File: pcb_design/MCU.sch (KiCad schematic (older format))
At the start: 17 parts, among them J9 SWD, SW1 BOOTLOADER, U1 STM32F40X_LQFP64, X2 ABM3B - 8MHz

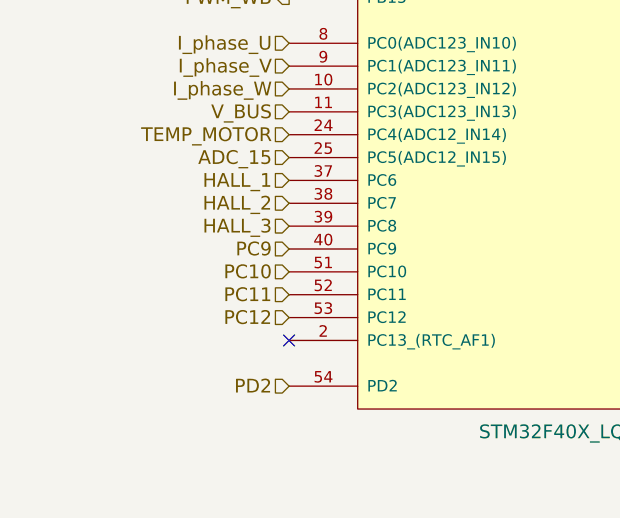
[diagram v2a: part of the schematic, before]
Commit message: Resolver routed. Added 12v regulator. The screw terminals were backwards(!). Started clearing up DRC markers.
Signed-off-by: Marcos Chaparro <mchaparro@paltatech.com>
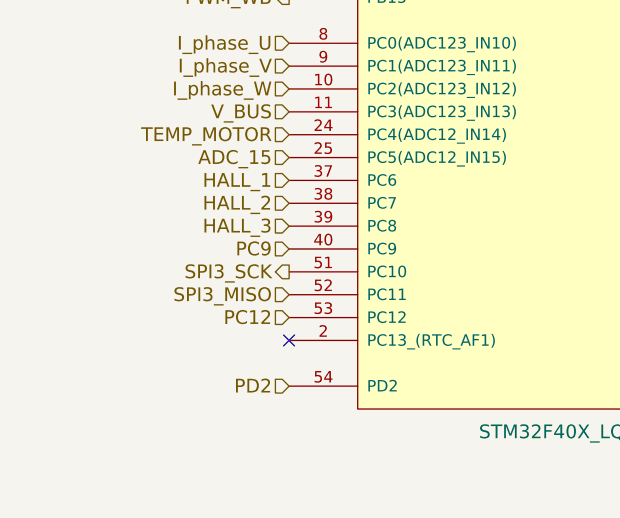
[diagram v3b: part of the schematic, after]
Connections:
- net PC10 renamed SPI3_SCK
- net PC11 renamed SPI3_MISO
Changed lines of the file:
@@
 I_phase_W
 Text HLabel 3650 5400 0    60   Input ~ 0
-PC11
-Text HLabel 3650 5500 0    60   Input ~ 0
-PC12
-Text HLabel 3650 5300 0    60   Input ~ 0
-PC10
+SPI3_MISO
+Text HLabel 3650 5300 0    60   Output ~ 0
+SPI3_SCK
 Text HLabel 3650 5200 0    60   Input ~ 0
 PC9
@@
 Text Notes 6000 2400 0    30   ~ 0
 remember it should be\npulled down if you want\nto enter bootloader
+Text HLabel 3650 5500 0    60   Input ~ 0
+PC12
 $EndSCHEMATC

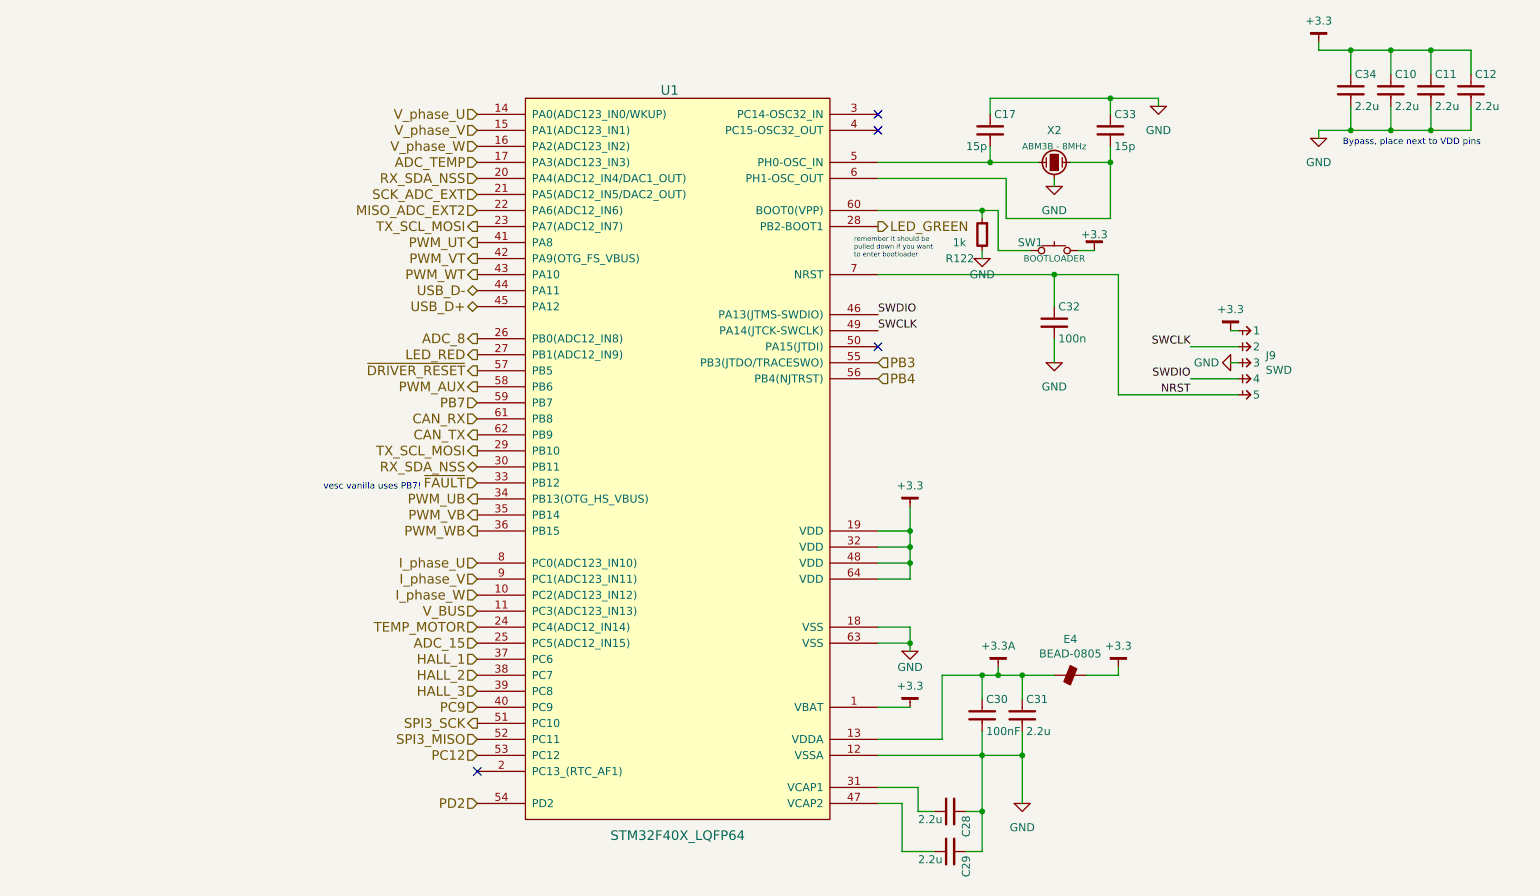
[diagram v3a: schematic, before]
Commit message: Routing complete. Added 3D models. No DRC errors, a few ERC warnings
Signed-off-by: Marcos Chaparro <mchaparro@paltatech.com>
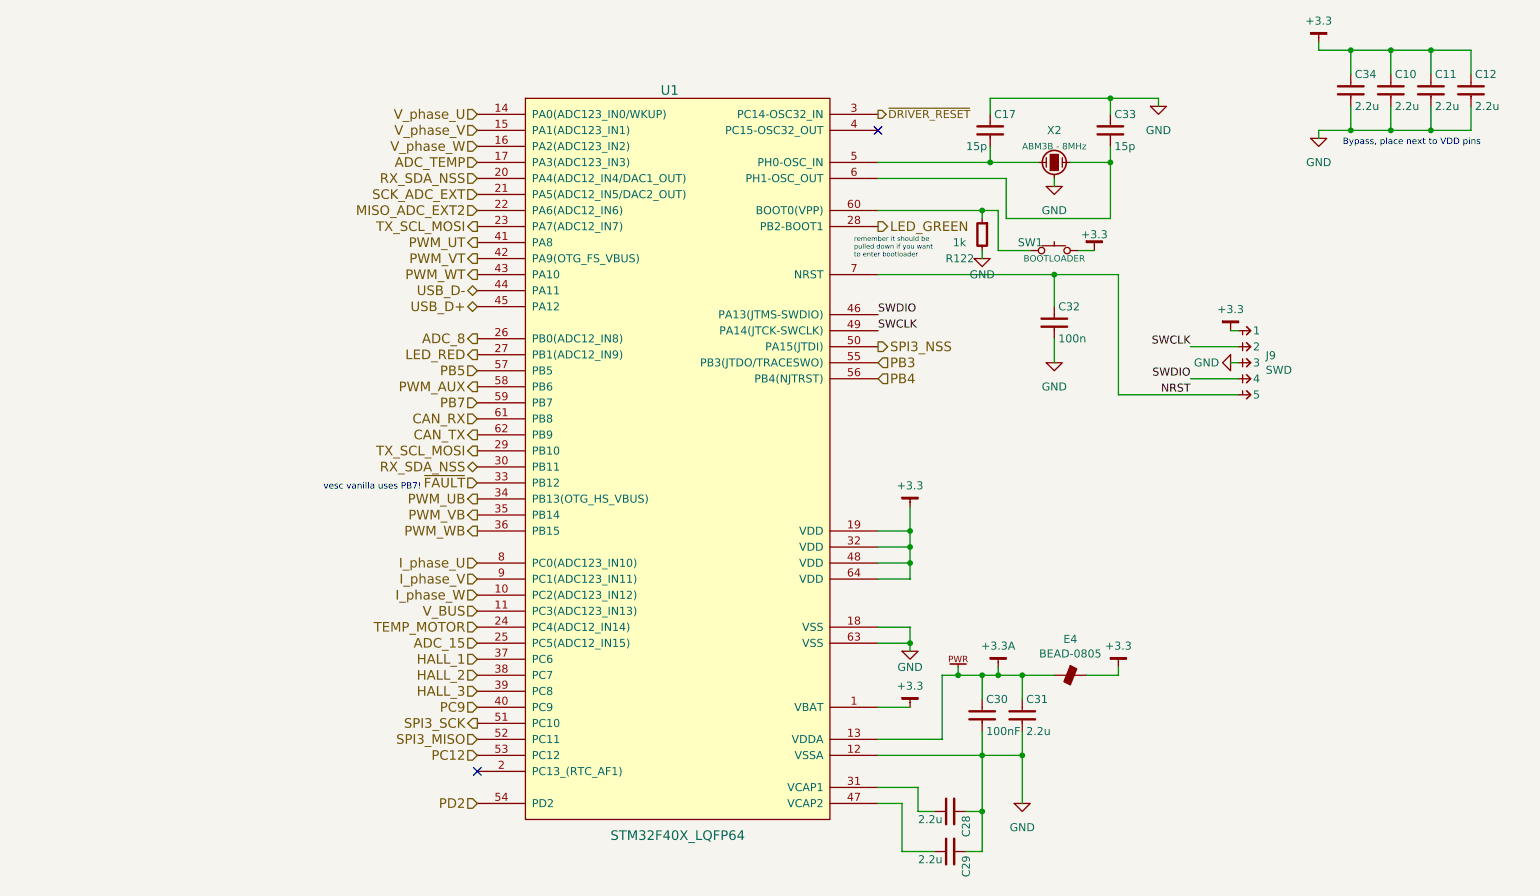
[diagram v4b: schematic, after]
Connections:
- net ~DRIVER_RESET: now also U1.3 (PC14-OSC32_IN); no longer U1.57 (PB5)
- net SPI3_NSS: now reaches U1.50 (PA15(JTDI))
- new net PB5: U1.57 (PB5)
- no-connect marks 4 -> 2
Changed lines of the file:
@@
 Text HLabel 3650 4600 0    60   Input ~ 0
 V_BUS
-Text HLabel 3650 3100 0    60   Output ~ 0
+Text HLabel 6150 1500 2    50   Output ~ 0
 ~DRIVER_RESET
 $Bitmap
@@
 Text HLabel 3650 1800 0    60   Input ~ 0
 ADC_TEMP
-NoConn ~ 6150 2950
-NoConn ~ 6150 1500
 NoConn ~ 6150 1600
 Wire Wire Line
@@
 Bypass, place next to VDD pins
 $Comp
-L GND #PWR0155
+L GND #PWR0169
 U 1 1 572D84DC
 P 7900 1450
-F 0 "#PWR0155" H 7900 1200 50  0001 C CNN
+F 0 "#PWR0169" H 7900 1200 50  0001 C CNN
 F 1 "GND" H 7900 1300 50  0000 C CNN
 F 2 "" H 7900 1450 60  0000 C CNN
@@
 $EndComp
 $Comp
-L GND #PWR0156
+L GND #PWR0170
 U 1 1 572D84DF
 P 7250 1950
-F 0 "#PWR0156" H 7250 1700 50  0001 C CNN
+F 0 "#PWR0170" H 7250 1700 50  0001 C CNN
 F 1 "GND" H 7250 1800 50  0000 C CNN
 F 2 "" H 7250 1950 60  0000 C CNN
@@
 $EndComp
 $Comp
-L GND #PWR0157
+L GND #PWR0171
 U 1 1 572D84E0
 P 6800 2400
-F 0 "#PWR0157" H 6800 2150 50  0001 C CNN
+F 0 "#PWR0171" H 6800 2150 50  0001 C CNN
 F 1 "GND" H 6800 2300 50  0000 C CNN
 F 2 "" H 6800 2400 60  0000 C CNN
@@
 $EndComp
 $Comp
-L GND #PWR0158
+L GND #PWR0172
 U 1 1 572D84E2
 P 7250 3050
-F 0 "#PWR0158" H 7250 2800 50  0001 C CNN
+F 0 "#PWR0172" H 7250 2800 50  0001 C CNN
 F 1 "GND" H 7250 2900 50  0000 C CNN
 F 2 "" H 7250 3050 60  0000 C CNN
@@
 	7250 3050 7250 2900
 $Comp
-L GND #PWR0159
+L GND #PWR0173
 U 1 1 572D84E3
 P 7050 5800
-F 0 "#PWR0159" H 7050 5550 50  0001 C CNN
+F 0 "#PWR0173" H 7050 5550 50  0001 C CNN
 F 1 "GND" H 7050 5650 50  0000 C CNN
 F 2 "" H 7050 5800 60  0000 C CNN
@@
 $EndComp
 $Comp
-L GND #PWR0160
+L GND #PWR0174
 U 1 1 572D84E4
 P 6350 4850
-F 0 "#PWR0160" H 6350 4600 50  0001 C CNN
+F 0 "#PWR0174" H 6350 4600 50  0001 C CNN
 F 1 "GND" H 6350 4750 50  0000 C CNN
 F 2 "" H 6350 4850 60  0000 C CNN
@@
 $EndComp
 $Comp
-L GND #PWR0161
+L GND #PWR0175
 U 1 1 572D84E9
 P 8900 1650
-F 0 "#PWR0161" H 8900 1400 50  0001 C CNN
+F 0 "#PWR0175" H 8900 1400 50  0001 C CNN
 F 1 "GND" H 8900 1500 50  0000 C CNN
 F 2 "" H 8900 1650 60  0000 C CNN
@@
 $EndComp
 $Comp
-L +3.3 #PWR0162
+L +3.3 #PWR0176
 U 1 1 588B6A3F
 P 8900 1050
-F 0 "#PWR0162" H 0   100 30  0001 C CNN
+F 0 "#PWR0176" H 0   100 30  0001 C CNN
 F 1 "+3.3" H 8900 1183 50  0000 C CNN
 F 2 "" H 0   50  60  0000 C CNN
@@
 Connection ~ 7250 2500
 $Comp
-L +3.3 #PWR0163
+L +3.3 #PWR0177
 U 1 1 588B6C25
 P 6350 3950
-F 0 "#PWR0163" H 6400 4000 30  0001 C CNN
+F 0 "#PWR0177" H 6400 4000 30  0001 C CNN
 F 1 "+3.3" H 6350 4083 50  0000 C CNN
 F 2 "" H 0   50  60  0000 C CNN
@@
 $EndComp
 $Comp
-L +3.3 #PWR0164
+L +3.3 #PWR0178
 U 1 1 588B6CC6
 P 7650 4950
-F 0 "#PWR0164" H 7700 5000 30  0001 C CNN
+F 0 "#PWR0178" H 7700 5000 30  0001 C CNN
 F 1 "+3.3" H 7650 5083 50  0000 C CNN
 F 2 "" H 0   50  60  0000 C CNN
@@
 $EndComp
 $Comp
-L +3.3 #PWR0165
+L +3.3 #PWR0179
 U 1 1 588B6D3A
 P 6350 5200
-F 0 "#PWR0165" H 6400 5250 30  0001 C CNN
+F 0 "#PWR0179" H 6400 5250 30  0001 C CNN
 F 1 "+3.3" H 6350 5333 50  0000 C CNN
 F 2 "" H -1300 300 60  0000 C CNN
@@
 $EndComp
 $Comp
-L +3.3A #PWR0166
+L +3.3A #PWR0180
 U 1 1 588B9943
 P 6900 4950
-F 0 "#PWR0166" H 6950 5000 30  0001 C CNN
+F 0 "#PWR0180" H 6950 5000 30  0001 C CNN
 F 1 "+3.3A" H 6900 5083 50  0000 C CNN
 F 2 "" H -900 -500 60  0000 C CNN
@@
 $EndComp
 $Comp
-L +3.3 #PWR0167
+L +3.3 #PWR0181
 U 1 1 5892B530
 P 8350 2850
-F 0 "#PWR0167" H -550 1900 30  0001 C CNN
+F 0 "#PWR0181" H -550 1900 30  0001 C CNN
 F 1 "+3.3" H 8350 2983 50  0000 C CNN
 F 2 "" H -550 1850 60  0000 C CNN
@@
 	8400 2950 8100 2950
 $Comp
-L GND #PWR0168
+L GND #PWR0182
 U 1 1 5892B905
 P 8350 3050
-F 0 "#PWR0168" H 8350 2800 50  0001 C CNN
+F 0 "#PWR0182" H 8350 2800 50  0001 C CNN
 F 1 "GND" V 8350 2900 50  0000 C CNN
 F 2 "" H 8350 3050 60  0000 C CNN
@@
 Connection ~ 6800 2100
 $Comp
-L +3.3 #PWR0169
+L +3.3 #PWR0183
 U 1 1 588E04AA
 P 7500 2350
-F 0 "#PWR0169" H -1400 1400 30  0001 C CNN
+F 0 "#PWR0183" H -1400 1400 30  0001 C CNN
 F 1 "+3.3" H 7500 2450 50  0000 C CNN
 F 2 "" H -1400 1350 60  0000 C CNN
@@
 Wire Wire Line
 	7500 2350 7400 2350
-Text HLabel 3650 1900 0    60   Input ~ 0
-RX_SDA_NSS
 Text HLabel 3650 2900 0    60   Output ~ 0
 ADC_8
@@
 Text HLabel 3650 5500 0    60   Input ~ 0
 PC12
+Text HLabel 6150 2950 2    60   Output ~ 0
+SPI3_NSS
+Text HLabel 3650 3100 0    60   Input ~ 0
+PB5
+Text HLabel 3650 1900 0    60   Input ~ 0
+RX_SDA_NSS
+$Comp
+L PWR_FLAG #PWR0184
+U 1 1 5893E14A
+P 6650 4950
+F 0 "#PWR0184" H 6700 5000 50  0001 C CNN
+F 1 "PWR_FLAG" H -200 200 50  0001 C CNN
+F 2 "" H -200 200 60  0000 C CNN
+F 3 "" H -200 200 60  0000 C CNN
+	1    6650 4950
+	1    0    0    -1
+$EndComp
+Wire Wire Line
+	6650 4950 6650 5000
+Connection ~ 6650 5000
 $EndSCHEMATC

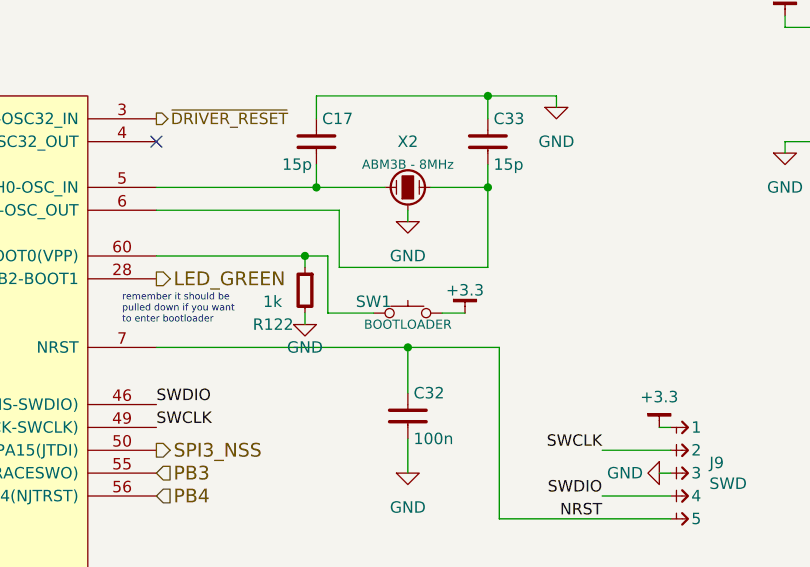
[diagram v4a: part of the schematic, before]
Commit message: Silkscreen logos, fixed swapped OCP inputs, added a button to enter bootloader,missing 3d model.
Signed-off-by: Marcos Chaparro <mchaparro@paltatech.com>
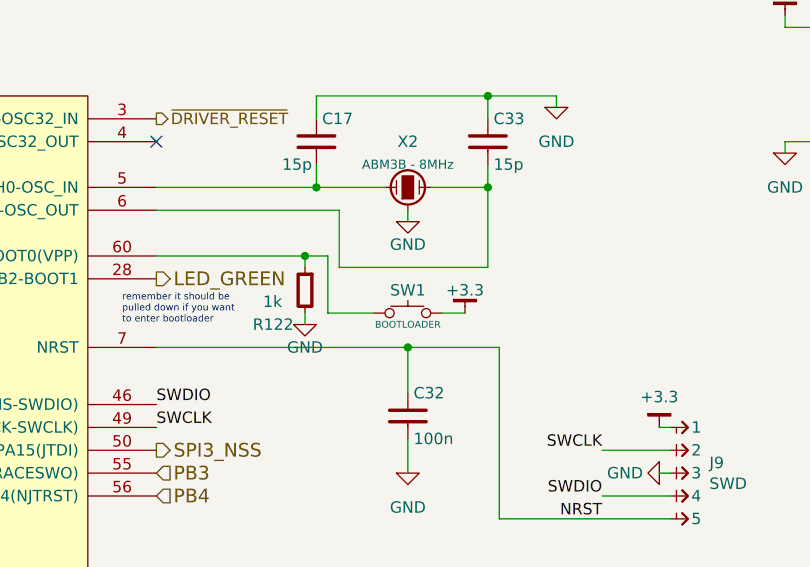
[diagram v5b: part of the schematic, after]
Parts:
- SW1: footprint (none) -> paltatech:SMD-Switch_B3U-1000-B; mfg# (none) -> B3U-1000P
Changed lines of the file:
@@
 Bypass, place next to VDD pins
 $Comp
-L GND #PWR0169
+L GND #PWR186
 U 1 1 572D84DC
 P 7900 1450
-F 0 "#PWR0169" H 7900 1200 50  0001 C CNN
+F 0 "#PWR186" H 7900 1200 50  0001 C CNN
 F 1 "GND" H 7900 1300 50  0000 C CNN
 F 2 "" H 7900 1450 60  0000 C CNN
@@
 $EndComp
 $Comp
-L GND #PWR0170
+L GND #PWR182
 U 1 1 572D84DF
 P 7250 1950
-F 0 "#PWR0170" H 7250 1700 50  0001 C CNN
-F 1 "GND" H 7250 1800 50  0000 C CNN
+F 0 "#PWR182" H 7250 1700 50  0001 C CNN
+F 1 "GND" H 7250 1850 50  0000 C CNN
 F 2 "" H 7250 1950 60  0000 C CNN
 F 3 "" H 7250 1950 60  0000 C CNN
@@
 $EndComp
 $Comp
-L GND #PWR0171
+L GND #PWR179
 U 1 1 572D84E0
 P 6800 2400
-F 0 "#PWR0171" H 6800 2150 50  0001 C CNN
+F 0 "#PWR179" H 6800 2150 50  0001 C CNN
 F 1 "GND" H 6800 2300 50  0000 C CNN
 F 2 "" H 6800 2400 60  0000 C CNN
@@
 $EndComp
 $Comp
-L GND #PWR0172
+L GND #PWR183
 U 1 1 572D84E2
 P 7250 3050
-F 0 "#PWR0172" H 7250 2800 50  0001 C CNN
+F 0 "#PWR183" H 7250 2800 50  0001 C CNN
 F 1 "GND" H 7250 2900 50  0000 C CNN
 F 2 "" H 7250 3050 60  0000 C CNN
@@
 	7250 3050 7250 2900
 $Comp
-L GND #PWR0173
+L GND #PWR181
 U 1 1 572D84E3
 P 7050 5800
-F 0 "#PWR0173" H 7050 5550 50  0001 C CNN
+F 0 "#PWR181" H 7050 5550 50  0001 C CNN
 F 1 "GND" H 7050 5650 50  0000 C CNN
 F 2 "" H 7050 5800 60  0000 C CNN
@@
 $EndComp
 $Comp
-L GND #PWR0174
+L GND #PWR176
 U 1 1 572D84E4
 P 6350 4850
-F 0 "#PWR0174" H 6350 4600 50  0001 C CNN
+F 0 "#PWR176" H 6350 4600 50  0001 C CNN
 F 1 "GND" H 6350 4750 50  0000 C CNN
 F 2 "" H 6350 4850 60  0000 C CNN
@@
 $EndComp
 $Comp
-L GND #PWR0175
+L GND #PWR190
 U 1 1 572D84E9
 P 8900 1650
-F 0 "#PWR0175" H 8900 1400 50  0001 C CNN
+F 0 "#PWR190" H 8900 1400 50  0001 C CNN
 F 1 "GND" H 8900 1500 50  0000 C CNN
 F 2 "" H 8900 1650 60  0000 C CNN
@@
 $EndComp
 $Comp
-L +3.3 #PWR0176
+L +3.3 #PWR189
 U 1 1 588B6A3F
 P 8900 1050
-F 0 "#PWR0176" H 0   100 30  0001 C CNN
+F 0 "#PWR189" H 0   100 30  0001 C CNN
 F 1 "+3.3" H 8900 1183 50  0000 C CNN
 F 2 "" H 0   50  60  0000 C CNN
@@
 Connection ~ 7250 2500
 $Comp
-L +3.3 #PWR0177
+L +3.3 #PWR175
 U 1 1 588B6C25
 P 6350 3950
-F 0 "#PWR0177" H 6400 4000 30  0001 C CNN
+F 0 "#PWR175" H 6400 4000 30  0001 C CNN
 F 1 "+3.3" H 6350 4083 50  0000 C CNN
 F 2 "" H 0   50  60  0000 C CNN
@@
 $EndComp
 $Comp
-L +3.3 #PWR0178
+L +3.3 #PWR185
 U 1 1 588B6CC6
 P 7650 4950
-F 0 "#PWR0178" H 7700 5000 30  0001 C CNN
+F 0 "#PWR185" H 7700 5000 30  0001 C CNN
 F 1 "+3.3" H 7650 5083 50  0000 C CNN
 F 2 "" H 0   50  60  0000 C CNN
@@
 $EndComp
 $Comp
-L +3.3 #PWR0179
+L +3.3 #PWR177
 U 1 1 588B6D3A
 P 6350 5200
-F 0 "#PWR0179" H 6400 5250 30  0001 C CNN
+F 0 "#PWR177" H 6400 5250 30  0001 C CNN
 F 1 "+3.3" H 6350 5333 50  0000 C CNN
 F 2 "" H -1300 300 60  0000 C CNN
@@
 $EndComp
 $Comp
-L +3.3A #PWR0180
+L +3.3A #PWR180
 U 1 1 588B9943
 P 6900 4950
-F 0 "#PWR0180" H 6950 5000 30  0001 C CNN
+F 0 "#PWR180" H 6950 5000 30  0001 C CNN
 F 1 "+3.3A" H 6900 5083 50  0000 C CNN
 F 2 "" H -900 -500 60  0000 C CNN
@@
 $EndComp
 $Comp
-L +3.3 #PWR0181
+L +3.3 #PWR187
 U 1 1 5892B530
 P 8350 2850
-F 0 "#PWR0181" H -550 1900 30  0001 C CNN
+F 0 "#PWR187" H -550 1900 30  0001 C CNN
 F 1 "+3.3" H 8350 2983 50  0000 C CNN
 F 2 "" H -550 1850 60  0000 C CNN
@@
 	8400 2950 8100 2950
 $Comp
-L GND #PWR0182
+L GND #PWR188
 U 1 1 5892B905
 P 8350 3050
-F 0 "#PWR0182" H 8350 2800 50  0001 C CNN
+F 0 "#PWR188" H 8350 2800 50  0001 C CNN
 F 1 "GND" V 8350 2900 50  0000 C CNN
 F 2 "" H 8350 3050 60  0000 C CNN
@@
 Wire Wire Line
 	6800 2100 6800 2150
-$Comp
-L PUSH SW1
-U 1 1 588E02FB
-P 7250 2350
-F 0 "SW1" H 7100 2400 50  0000 C CNN
-F 1 "BOOTLOADER" H 7250 2300 40  0000 C CNN
-F 2 "" H 100 0   60  0000 C CNN
-F 3 "" H 100 0   60  0000 C CNN
-	1    7250 2350
-	1    0    0    -1
-$EndComp
 Wire Wire Line
 	6900 2100 6900 2350
@@
 Connection ~ 6800 2100
 $Comp
-L +3.3 #PWR0183
+L +3.3 #PWR184
 U 1 1 588E04AA
 P 7500 2350
-F 0 "#PWR0183" H -1400 1400 30  0001 C CNN
+F 0 "#PWR184" H -1400 1400 30  0001 C CNN
 F 1 "+3.3" H 7500 2450 50  0000 C CNN
 F 2 "" H -1400 1350 60  0000 C CNN
@@
 RX_SDA_NSS
 $Comp
-L PWR_FLAG #PWR0184
+L PWR_FLAG #PWR178
 U 1 1 5893E14A
 P 6650 4950
-F 0 "#PWR0184" H 6700 5000 50  0001 C CNN
+F 0 "#PWR178" H 6700 5000 50  0001 C CNN
 F 1 "PWR_FLAG" H -200 200 50  0001 C CNN
 F 2 "" H -200 200 60  0000 C CNN
@@
 	6650 4950 6650 5000
 Connection ~ 6650 5000
+$Comp
+L PUSH SW1
+U 1 1 58963AE7
+P 7250 2350
+F 0 "SW1" H 7250 2450 50  0000 C CNN
+F 1 "BOOTLOADER" H 7250 2300 30  0000 C CNN
+F 2 "paltatech:SMD-Switch_B3U-1000-B" H 7250 2486 60  0001 C CNN
+F 3 "" H 50  0   60  0000 C CNN
+F 4 "B3U-1000P" H 7250 2350 60  0001 C CNN "mfg#"
+	1    7250 2350
+	1    0    0    -1
+$EndComp
 $EndSCHEMATC
